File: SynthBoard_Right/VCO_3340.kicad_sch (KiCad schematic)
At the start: 49 parts, among them IC4 AS321KTR-G1, IC5 V3340M, SW1 MFP_240

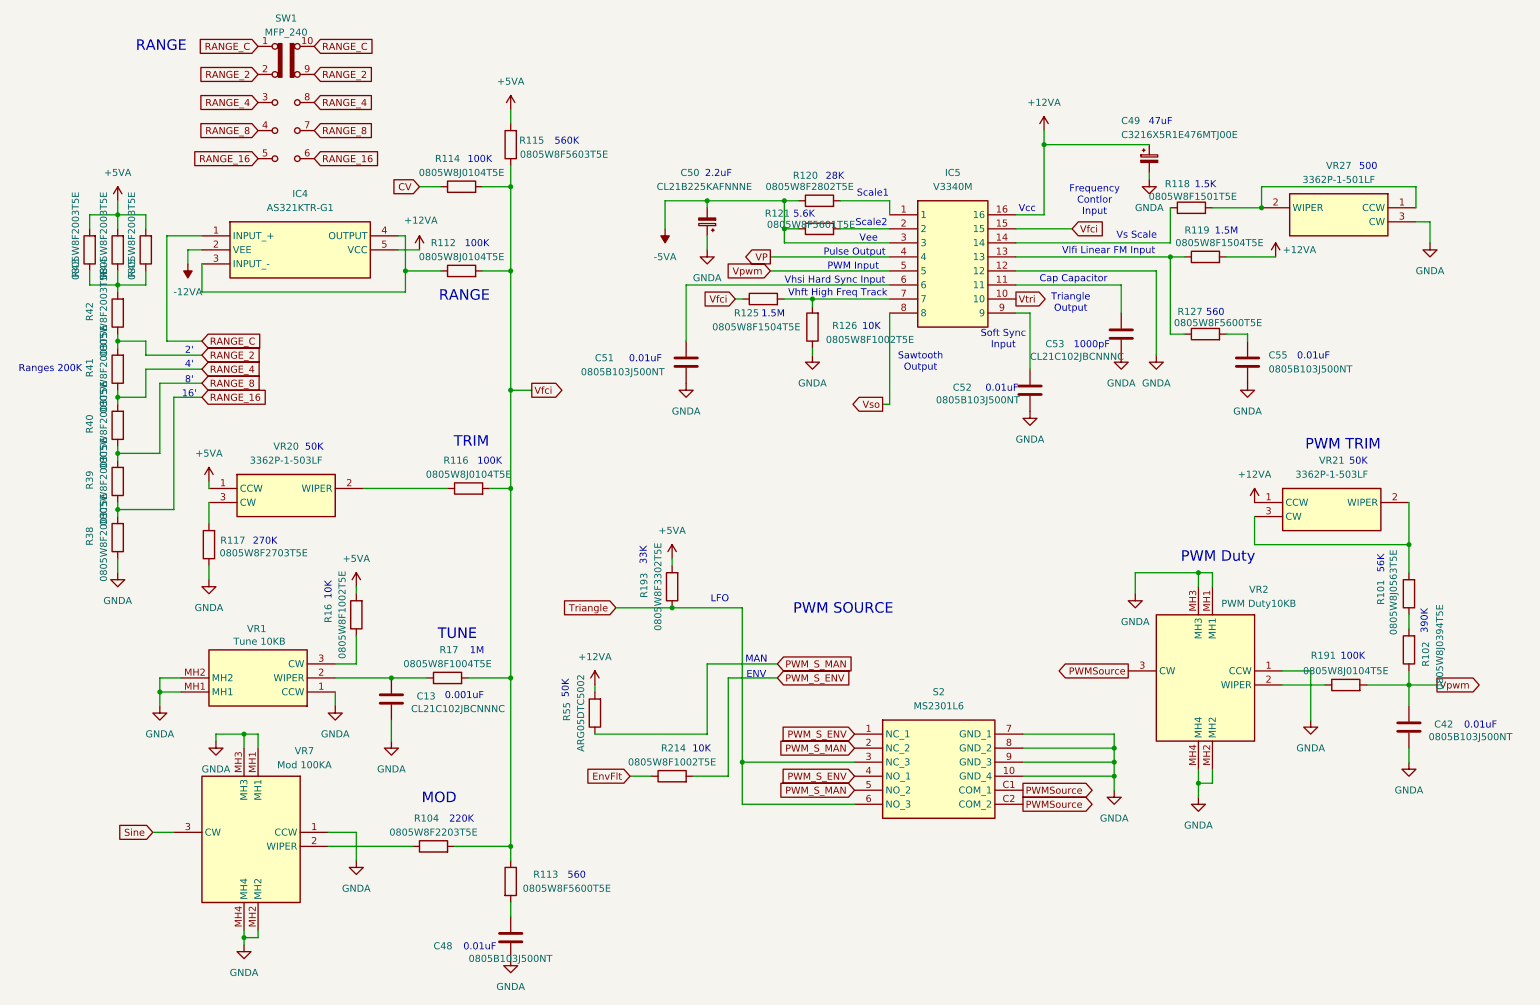
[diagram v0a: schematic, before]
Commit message: SynthBoard
Rightを配置済
Leftの配線ミスを修正
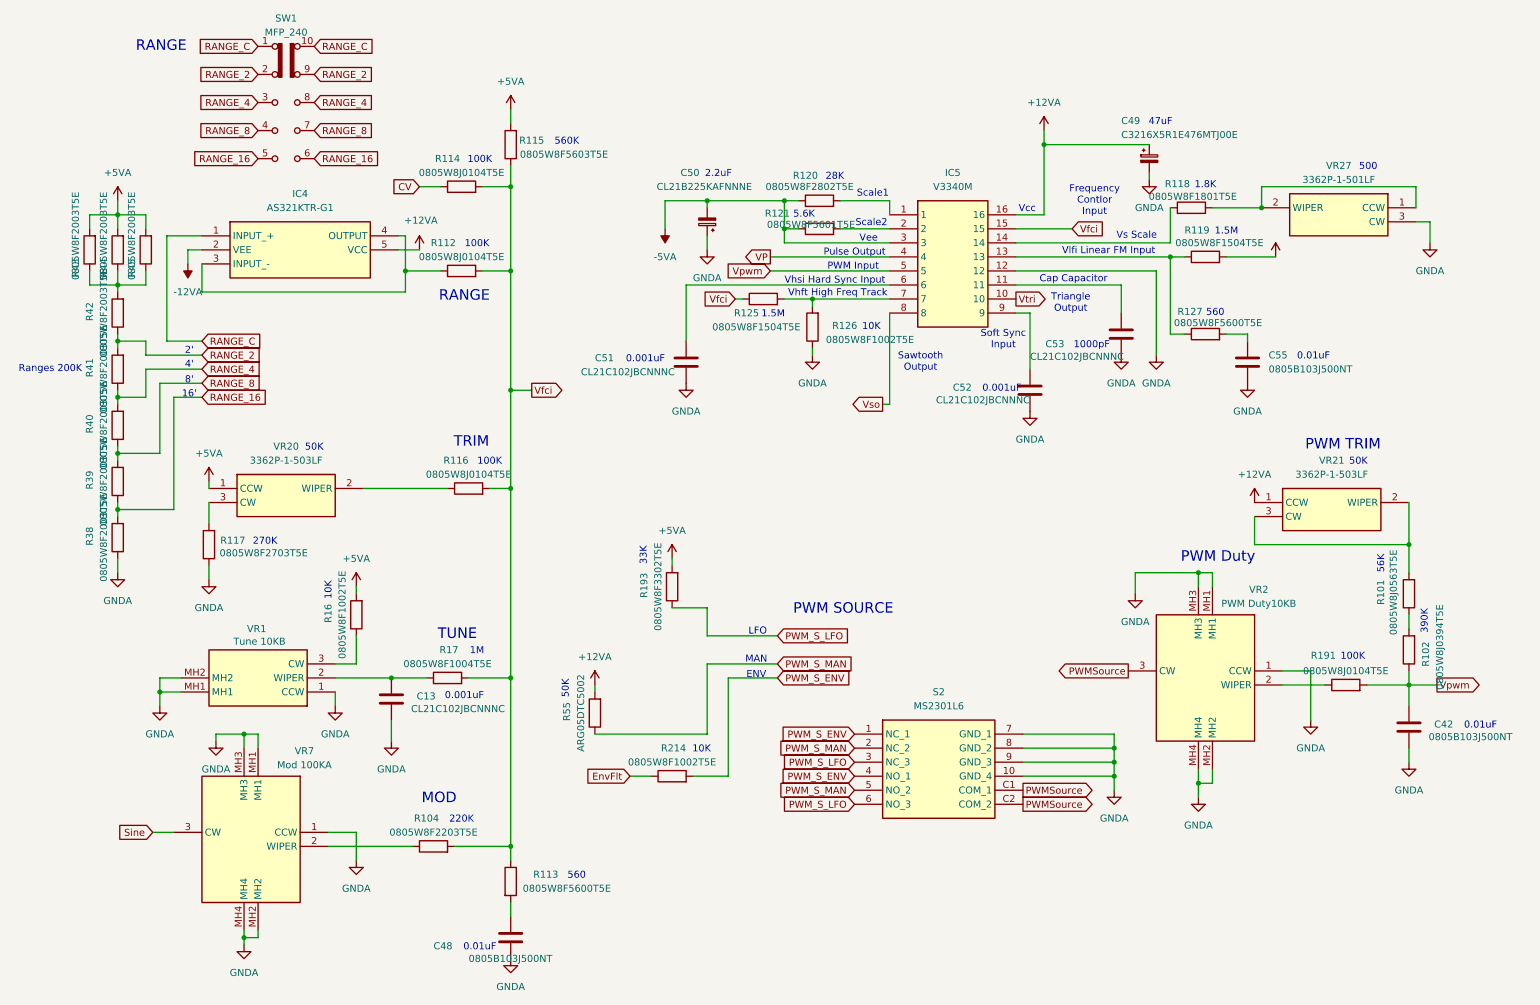
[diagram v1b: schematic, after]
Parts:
- C51, C52: value 0805B103J500NT -> CL21C102JBCNNNC
- R118: value 0805W8F1501T5E -> 0805W8F1801T5E
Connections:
- net Triangle renamed PWM_S_LFO
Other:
- note added: "1.8K"
- note removed: "1.5K"
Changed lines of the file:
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@@
 	(text "LFO"
 		(exclude_from_sim no)
-		(at 145.796 117.856 0)
+		(at 152.654 123.698 0)
 		(effects
 			(font
@@
 		)
 	)
-	(text "1.5K"
+	(text "1.8K"
 		(exclude_from_sim no)
 		(at 233.68 42.926 0)
@@
 		)
 	)
-	(text "0.01uF"
+	(text "0.001uF"
 		(exclude_from_sim no)
 		(at 196.85 79.756 0)
@@
 		)
 	)
-	(text "0.01uF"
+	(text "0.001uF"
 		(exclude_from_sim no)
 		(at 132.334 74.422 0)
@@
 	)
 	(junction
-		(at 137.16 119.38)
-		(diameter 0)
-		(color 0 0 0 0)
-	)
-	(junction
-		(at 149.86 147.32)
-		(diameter 0)
-		(color 0 0 0 0)
-	)
-	(junction
 		(at 88.9 58.42)
 		(diameter 0)
@@
 	(wire
 		(pts
-			(xy 149.86 147.32) (xy 149.86 119.38)
+			(xy 162.56 63.5) (xy 176.53 63.5)
 		)
 		(stroke
@@
 	(wire
 		(pts
-			(xy 162.56 63.5) (xy 176.53 63.5)
+			(xy 53.34 96.52) (xy 53.34 97.79)
 		)
 		(stroke
@@
 	(wire
 		(pts
-			(xy 53.34 96.52) (xy 53.34 97.79)
+			(xy 137.16 110.49) (xy 137.16 111.76)
 		)
 		(stroke
@@
 	(wire
 		(pts
-			(xy 137.16 110.49) (xy 137.16 111.76)
+			(xy 36.83 60.96) (xy 36.83 62.23)
 		)
 		(stroke
@@
 	(wire
 		(pts
-			(xy 36.83 60.96) (xy 36.83 62.23)
+			(xy 46.99 101.6) (xy 46.99 81.28)
 		)
 		(stroke
@@
 	(wire
 		(pts
-			(xy 46.99 101.6) (xy 46.99 81.28)
+			(xy 41.91 71.12) (xy 41.91 73.66)
 		)
 		(stroke
@@
 	(wire
 		(pts
-			(xy 41.91 71.12) (xy 41.91 73.66)
+			(xy 199.39 55.88) (xy 227.33 55.88)
 		)
 		(stroke
@@
 	(wire
 		(pts
-			(xy 199.39 55.88) (xy 227.33 55.88)
+			(xy 143.51 124.46) (xy 156.21 124.46)
 		)
 		(stroke
@@
 	(wire
 		(pts
+			(xy 143.51 119.38) (xy 143.51 124.46)
+		)
+		(stroke
+			(width 0)
+			(type default)
+		)
+	)
+	(wire
+		(pts
 			(xy 143.51 45.72) (xy 157.48 45.72)
 		)
@@
 	(wire
 		(pts
-			(xy 170.18 154.94) (xy 149.86 154.94)
-		)
-		(stroke
-			(width 0)
-			(type default)
-		)
-	)
-	(wire
-		(pts
 			(xy 53.34 111.76) (xy 53.34 114.3)
 		)
@@
 	(wire
 		(pts
-			(xy 127 119.38) (xy 137.16 119.38)
-		)
-		(stroke
-			(width 0)
-			(type default)
-		)
-	)
-	(wire
-		(pts
 			(xy 218.44 60.96) (xy 218.44 66.04)
 		)
@@
 	(wire
 		(pts
-			(xy 107.95 29.21) (xy 107.95 31.75)
+			(xy 137.16 119.38) (xy 143.51 119.38)
 		)
 		(stroke
@@
 	(wire
 		(pts
-			(xy 48.26 134.62) (xy 44.45 134.62)
+			(xy 107.95 29.21) (xy 107.95 31.75)
 		)
 		(stroke
@@
 	(wire
 		(pts
-			(xy 223.52 40.64) (xy 223.52 41.91)
+			(xy 48.26 134.62) (xy 44.45 134.62)
 		)
 		(stroke
@@
 	(wire
 		(pts
-			(xy 170.18 147.32) (xy 149.86 147.32)
+			(xy 223.52 40.64) (xy 223.52 41.91)
 		)
 		(stroke
@@
 	(wire
 		(pts
-			(xy 149.86 154.94) (xy 149.86 147.32)
-		)
-		(stroke
-			(width 0)
-			(type default)
-		)
-	)
-	(wire
-		(pts
 			(xy 107.95 162.56) (xy 107.95 132.08)
 		)
@@
 	(wire
 		(pts
-			(xy 149.86 119.38) (xy 137.16 119.38)
-		)
-		(stroke
-			(width 0)
-			(type default)
-		)
-	)
-	(wire
-		(pts
 			(xy 43.18 160.02) (xy 46.99 160.02)
 		)
@@
 		)
 	)
+	(global_label "PWM_S_LFO"
+		(shape input)
+		(at 170.18 154.94 180)
+		(fields_autoplaced yes)
+		(effects
+			(font
+				(size 1.27 1.27)
+			)
+			(justify right)
+		)
+		(property "Intersheetrefs" "${INTERSHEET_REFS}"
+			(at 156.4301 154.94 0)
+			(effects
+				(font
+					(size 1.27 1.27)
+				)
+				(justify right)
+				(hide yes)
+			)
+		)
+	)
 	(global_label "RANGE_8"
 		(shape input)
@@
 		)
 	)
-	(global_label "Triangle"
-		(shape input)
-		(at 127 119.38 180)
-		(fields_autoplaced yes)
-		(effects
-			(font
-				(size 1.27 1.27)
-			)
-			(justify right)
-		)
-		(property "Intersheetrefs" "${INTERSHEET_REFS}"
-			(at 116.4554 119.38 0)
-			(effects
-				(font
-					(size 1.27 1.27)
-				)
-				(justify right)
-				(hide yes)
-			)
-		)
-	)
 	(global_label "PWM_S_ENV"
 		(shape input)
@@
 		)
 	)
+	(global_label "PWM_S_LFO"
+		(shape input)
+		(at 170.18 147.32 180)
+		(fields_autoplaced yes)
+		(effects
+			(font
+				(size 1.27 1.27)
+			)
+			(justify right)
+		)
+		(property "Intersheetrefs" "${INTERSHEET_REFS}"
+			(at 156.4301 147.32 0)
+			(effects
+				(font
+					(size 1.27 1.27)
+				)
+				(justify right)
+				(hide yes)
+			)
+		)
+	)
 	(global_label "PWM_S_ENV"
 		(shape input)
@@
 		)
 	)
+	(global_label "PWM_S_LFO"
+		(shape input)
+		(at 156.21 124.46 0)
+		(fields_autoplaced yes)
+		(effects
+			(font
+				(size 1.27 1.27)
+			)
+			(justify left)
+		)
+		(property "Intersheetrefs" "${INTERSHEET_REFS}"
+			(at 167.7827 124.46 0)
+			(effects
+				(font
+					(size 1.27 1.27)
+				)
+				(justify left)
+				(hide yes)
+			)
+		)
+	)
 	(global_label "Vfci"
 		(shape input)
@@
 			)
 		)
-		(property "Value" "0805W8F1501T5E"
+		(property "Value" "0805W8F1801T5E"
 			(at 231.394 44.958 90)
 			(effects
@@
 			)
 		)
-		(property "Value" "0805B103J500NT"
+		(property "Value" "CL21C102JBCNNNC"
 			(at 184.912 81.788 0)
 			(effects
@@
 			)
 		)
-		(property "Value" "0805B103J500NT"
+		(property "Value" "CL21C102JBCNNNC"
 			(at 120.65 76.708 0)
 			(effects
@@
 	)
 	(symbol
-		(lib_id "power:+12VA")
-		(at 246.38 55.88 0)
-		(unit 1)
-		(exclude_from_sim no)
-		(in_bom yes)
-		(on_board yes)
-		(dnp no)
-		(property "Reference" "#PWR03"
-			(at 246.38 59.69 0)
-			(effects
-				(font
-					(size 1.27 1.27)
-				)
-				(hide yes)
-			)
-		)
-		(property "Value" "+12VA"
-			(at 250.698 54.61 0)
-			(effects
-				(font
-					(size 1.27 1.27)
-				)
-			)
-		)
-		(property "Footprint" ""
-			(at 246.38 55.88 0)
-			(effects
-				(font
-					(size 1.27 1.27)
-				)
-				(hide yes)
-			)
-		)
-		(property "Datasheet" ""
-			(at 246.38 55.88 0)
-			(effects
-				(font
-					(size 1.27 1.27)
-				)
-				(hide yes)
-			)
-		)
-		(property "Description" "Power symbol creates a global label with name \"+12VA\""
-			(at 246.38 55.88 0)
-			(effects
-				(font
-					(size 1.27 1.27)
-				)
-				(hide yes)
-			)
-		)
-		(pin "1"
-		)
-		(instances
-			(project "SynthBoard"
-				(path "/92765e2f-a998-485f-b610-76a9d5b50cba/31ade73f-3a23-4ba6-8fdd-ae7b8a426ce4"
-					(reference "#PWR03")
-					(unit 1)
-				)
-			)
-		)
-	)
-	(symbol
 		(lib_id "Device:C_Polarized_Small")
 		(at 223.52 38.1 0)
@@
 					(unit 1)
 				)
+			)
+		)
+	)
+	(symbol
+		(lib_id "power:+12VA")
+		(at 246.38 55.88 0)
+		(unit 1)
+		(exclude_from_sim no)
+		(in_bom yes)
+		(on_board yes)
+		(dnp no)
+		(fields_autoplaced yes)
+		(property "Reference" "#PWR069"
+			(at 246.38 59.69 0)
+			(effects
+				(font
+					(size 1.27 1.27)
+				)
+				(hide yes)
+			)
+		)
+		(property "Value" "+12VA"
+			(at 246.38 50.8 0)
+			(effects
+				(font
+					(size 1.27 1.27)
+				)
+				(hide yes)
+			)
+		)
+		(property "Footprint" ""
+			(at 246.38 55.88 0)
+			(effects
+				(font
+					(size 1.27 1.27)
+				)
+				(hide yes)
+			)
+		)
+		(property "Datasheet" ""
+			(at 246.38 55.88 0)
+			(effects
+				(font
+					(size 1.27 1.27)
+				)
+				(hide yes)
+			)
+		)
+		(property "Description" "Power symbol creates a global label with name \"+12VA\""
+			(at 246.38 55.88 0)
+			(effects
+				(font
+					(size 1.27 1.27)
+				)
+				(hide yes)
+			)
+		)
+		(pin "1"
+		)
+		(instances
+			(project "SynthBoard"
+				(path "/92765e2f-a998-485f-b610-76a9d5b50cba/31ade73f-3a23-4ba6-8fdd-ae7b8a426ce4"
+					(reference "#PWR069")
+					(unit 1)
+				)
